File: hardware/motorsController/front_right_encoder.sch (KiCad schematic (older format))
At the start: 6 parts, among them Q1 Q_Photo_NPN

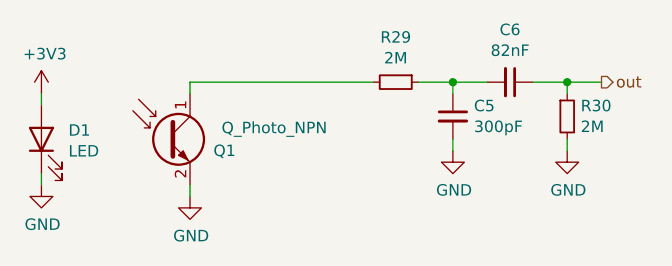
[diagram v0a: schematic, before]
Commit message: add three more encoders
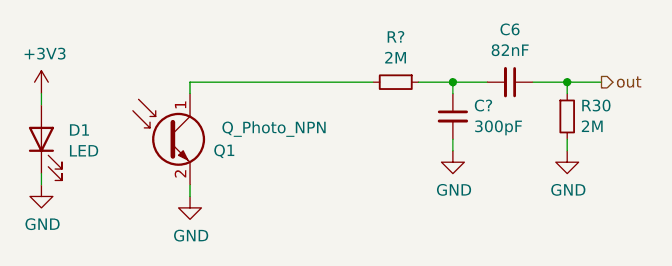
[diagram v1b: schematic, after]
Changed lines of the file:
@@
 $Descr A4 11693 8268
 encoding utf-8
-Sheet 6 6
+Sheet 9 9
 Title ""
 Date ""
@@
 U 1 1 5FB0A7B2
 P 1700 2350
-F 0 "D1" V 1739 2232 50  0000 R CNN
+AR Path="/5FB03879/5FB0A7B2" Ref="D1"  Part="1"
+AR Path="/5FBFC472/5FB0A7B2" Ref="D?"  Part="1"
+AR Path="/5FC04BEE/5FB0A7B2" Ref="D?"  Part="1"
+AR Path="/5FC04BF2/5FB0A7B2" Ref="D?"  Part="1"
+F 0 "D?" V 1739 2232 50  0000 R CNN
 F 1 "LED" V 1648 2232 50  0000 R CNN
 F 2 "Connector_PinSocket_2.54mm:PinSocket_1x02_P2.54mm_Vertical" H 1700 2350 50  0001 C CNN
@@
 U 1 1 5FB0A7B8
 P 2250 2350
-F 0 "Q1" H 2550 2300 50  0000 R CNN
+AR Path="/5FB03879/5FB0A7B8" Ref="Q1"  Part="1"
+AR Path="/5FBFC472/5FB0A7B8" Ref="Q?"  Part="1"
+AR Path="/5FC04BEE/5FB0A7B8" Ref="Q?"  Part="1"
+AR Path="/5FC04BF2/5FB0A7B8" Ref="Q?"  Part="1"
+F 0 "Q?" H 2550 2300 50  0000 R CNN
 F 1 "Q_Photo_NPN" H 2950 2400 50  0000 R CNN
 F 2 "Connector_PinSocket_2.54mm:PinSocket_1x02_P2.54mm_Vertical" H 2450 2450 50  0001 C CNN
@@
 U 1 1 5FB0A7BE
 P 1700 2550
-F 0 "#PWR0123" H 1700 2300 50  0001 C CNN
+AR Path="/5FB03879/5FB0A7BE" Ref="#PWR0123"  Part="1"
+AR Path="/5FBFC472/5FB0A7BE" Ref="#PWR?"  Part="1"
+AR Path="/5FC04BEE/5FB0A7BE" Ref="#PWR?"  Part="1"
+AR Path="/5FC04BF2/5FB0A7BE" Ref="#PWR?"  Part="1"
+F 0 "#PWR?" H 1700 2300 50  0001 C CNN
 F 1 "GND" H 1705 2377 50  0000 C CNN
 F 2 "" H 1700 2550 50  0001 C CNN
@@
 U 1 1 5FB0A7C5
 P 1700 2150
-F 0 "#PWR0124" H 1700 2000 50  0001 C CNN
+AR Path="/5FB03879/5FB0A7C5" Ref="#PWR0124"  Part="1"
+AR Path="/5FBFC472/5FB0A7C5" Ref="#PWR?"  Part="1"
+AR Path="/5FC04BEE/5FB0A7C5" Ref="#PWR?"  Part="1"
+AR Path="/5FC04BF2/5FB0A7C5" Ref="#PWR?"  Part="1"
+F 0 "#PWR?" H 1700 2000 50  0001 C CNN
 F 1 "+3V3" H 1715 2323 50  0000 C CNN
 F 2 "" H 1700 2150 50  0001 C CNN
@@
 U 1 1 5FB0A7CC
 P 2350 2600
-F 0 "#PWR0125" H 2350 2350 50  0001 C CNN
+AR Path="/5FB03879/5FB0A7CC" Ref="#PWR0125"  Part="1"
+AR Path="/5FBFC472/5FB0A7CC" Ref="#PWR?"  Part="1"
+AR Path="/5FC04BEE/5FB0A7CC" Ref="#PWR?"  Part="1"
+AR Path="/5FC04BF2/5FB0A7CC" Ref="#PWR?"  Part="1"
+F 0 "#PWR?" H 2350 2350 50  0001 C CNN
 F 1 "GND" H 2355 2427 50  0000 C CNN
 F 2 "" H 2350 2600 50  0001 C CNN
@@
 AR Path="/5FB0A7D3" Ref="C?"  Part="1"
 AR Path="/5FB03879/5FB0A7D3" Ref="C5"  Part="1"
-F 0 "C5" H 3592 2296 50  0000 L CNN
+AR Path="/5FBFC472/5FB0A7D3" Ref="C?"  Part="1"
+AR Path="/5FC04BEE/5FB0A7D3" Ref="C?"  Part="1"
+AR Path="/5FC04BF2/5FB0A7D3" Ref="C?"  Part="1"
+F 0 "C?" H 3592 2296 50  0000 L CNN
 F 1 "300pF" H 3592 2205 50  0000 L CNN
 F 2 "Capacitor_SMD:C_0805_2012Metric" H 3500 2250 50  0001 C CNN
@@
 AR Path="/5FB0A7D9" Ref="R?"  Part="1"
 AR Path="/5FB03879/5FB0A7D9" Ref="R29"  Part="1"
-F 0 "R29" V 3054 2100 50  0000 C CNN
+AR Path="/5FBFC472/5FB0A7D9" Ref="R?"  Part="1"
+AR Path="/5FC04BEE/5FB0A7D9" Ref="R?"  Part="1"
+AR Path="/5FC04BF2/5FB0A7D9" Ref="R?"  Part="1"
+F 0 "R?" V 3054 2100 50  0000 C CNN
 F 1 "2M" V 3145 2100 50  0000 C CNN
 F 2 "Resistor_SMD:R_0805_2012Metric" H 3250 2100 50  0001 C CNN
@@
 U 1 1 5FB0B2E6
 P 3500 2400
-F 0 "#PWR0126" H 3500 2150 50  0001 C CNN
+AR Path="/5FB03879/5FB0B2E6" Ref="#PWR0126"  Part="1"
+AR Path="/5FBFC472/5FB0B2E6" Ref="#PWR?"  Part="1"
+AR Path="/5FC04BEE/5FB0B2E6" Ref="#PWR?"  Part="1"
+AR Path="/5FC04BF2/5FB0B2E6" Ref="#PWR?"  Part="1"
+F 0 "#PWR?" H 3500 2150 50  0001 C CNN
 F 1 "GND" H 3505 2227 50  0000 C CNN
 F 2 "" H 3500 2400 50  0001 C CNN
@@
 U 1 1 5FB0F088
 P 3750 2100
-F 0 "C6" V 3521 2100 50  0000 C CNN
+AR Path="/5FB03879/5FB0F088" Ref="C6"  Part="1"
+AR Path="/5FBFC472/5FB0F088" Ref="C?"  Part="1"
+AR Path="/5FC04BEE/5FB0F088" Ref="C?"  Part="1"
+AR Path="/5FC04BF2/5FB0F088" Ref="C?"  Part="1"
+F 0 "C?" V 3521 2100 50  0000 C CNN
 F 1 "82nF" V 3612 2100 50  0000 C CNN
 F 2 "Capacitor_SMD:C_1206_3216Metric" H 3750 2100 50  0001 C CNN
@@
 U 1 1 5FB110C4
 P 4000 2250
-F 0 "R30" H 4059 2296 50  0000 L CNN
+AR Path="/5FB03879/5FB110C4" Ref="R30"  Part="1"
+AR Path="/5FBFC472/5FB110C4" Ref="R?"  Part="1"
+AR Path="/5FC04BEE/5FB110C4" Ref="R?"  Part="1"
+AR Path="/5FC04BF2/5FB110C4" Ref="R?"  Part="1"
+F 0 "R?" H 4059 2296 50  0000 L CNN
 F 1 "2M" H 4059 2205 50  0000 L CNN
 F 2 "Resistor_SMD:R_0805_2012Metric" H 4000 2250 50  0001 C CNN
@@
 U 1 1 5FB12EE4
 P 4000 2400
-F 0 "#PWR0127" H 4000 2150 50  0001 C CNN
+AR Path="/5FB03879/5FB12EE4" Ref="#PWR0127"  Part="1"
+AR Path="/5FBFC472/5FB12EE4" Ref="#PWR?"  Part="1"
+AR Path="/5FC04BEE/5FB12EE4" Ref="#PWR?"  Part="1"
+AR Path="/5FC04BF2/5FB12EE4" Ref="#PWR?"  Part="1"
+F 0 "#PWR?" H 4000 2150 50  0001 C CNN
 F 1 "GND" H 4005 2227 50  0000 C CNN
 F 2 "" H 4000 2400 50  0001 C CNN
